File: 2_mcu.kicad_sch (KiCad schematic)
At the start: 24 parts, among them J1 SWD TagConnect

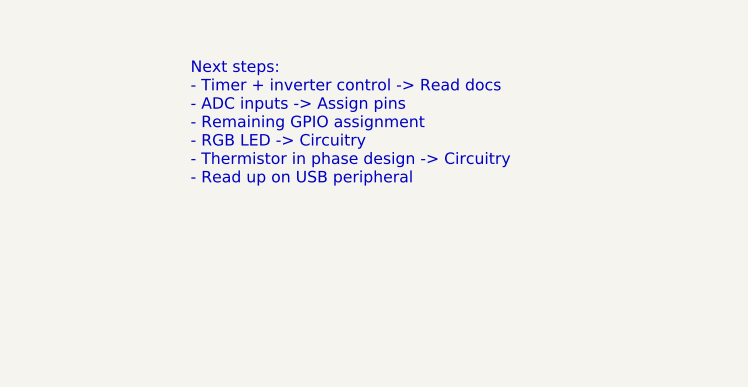
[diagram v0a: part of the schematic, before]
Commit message: verified Timer 1 functionality for motor control
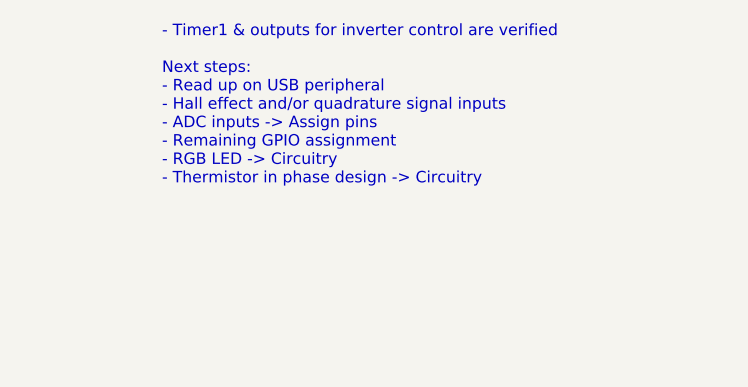
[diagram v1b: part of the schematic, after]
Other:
- note added: "- Timer1 & outputs for inverter control are verified Next steps: - Read up on USB peripheral - Hall effect and/or quadrature signal inputs - ADC inputs -> Assign pins - Remaining GPIO assignment - RGB LED -> Circuitry - Thermistor in phase design -> Circuitry"
- note removed: "Next steps: - Timer + inverter control -> Read docs - ADC inputs -> Assign pins - Remaining GPIO assignment - RGB LED -> Circuitry - Thermistor in phase design -> Circuitry - Read up on USB peripheral"
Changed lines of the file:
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@@
     (effects (font (size 1.6 1.6) italic) (justify left bottom))
   )
-  (text "Next steps:\n- Timer + inverter control -> Read docs\n- ADC inputs -> Assign pins\n- Remaining GPIO assignment\n- RGB LED -> Circuitry\n- Thermistor in phase design -> Circuitry\n- Read up on USB peripheral"
-    (at 234.315 34.925 0)
+  (text "- Timer1 & outputs for inverter control are verified\n\nNext steps:\n- Read up on USB peripheral\n- Hall effect and/or quadrature signal inputs\n- ADC inputs -> Assign pins\n- Remaining GPIO assignment\n- RGB LED -> Circuitry\n- Thermistor in phase design -> Circuitry\n"
+    (at 231.14 34.925 0)
     (effects (font (size 1.27 1.27)) (justify left bottom))
   )

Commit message: feat: USB circuitry
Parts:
- removed D1: ESDALC6V1W5, symbol Power_Protection:ESDALC6V1W5
- added D2: ESDA6V1-5SC6, Package_TO_SOT_SMD:SOT-23-6, symbol Power_Protection:ESDA6V1-5SC6
- added R1: 50R, symbol Device:R_Small
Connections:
- net +3.3V: now also D2.6 (IO5)
- net GND: now also D2.2 (GND); no longer J1.6 (SWO)
- net SYS_SWDIO: now also R1.1
- net at J1.2 (SWDIO), R?.2: now also D2.3 (IO2)
- net at J1.4 (SWCLK), R?.2: now also D2.4 (IO3)
- net at J1.3 (~{RESET}), R?.2: now also D2.5 (IO4)
- new net: D2.1 (IO1), J1.6 (SWO), R1.2
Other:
- note added: "- Timer1 & outputs for inverter control are verified Next steps: - Hall effect and/or quadrature signal inputs - ADC inputs -> Assign pins - Remaining GPIO assignment - RGB LED -> Circuitry - Thermistor in phase design -> Circuitry"
- note removed: "- Timer1 & outputs for inverter control are verified Next steps: - Read up on USB peripheral - Hall effect and/or quadrature signal inputs - ADC inputs -> Assign pins - Remaining GPIO assignment - RGB LED -> Circuitry - Thermistor in phase design -> Circuitry"
- moved on the sheet: C?, L?, R?, SW?, U?, Y?

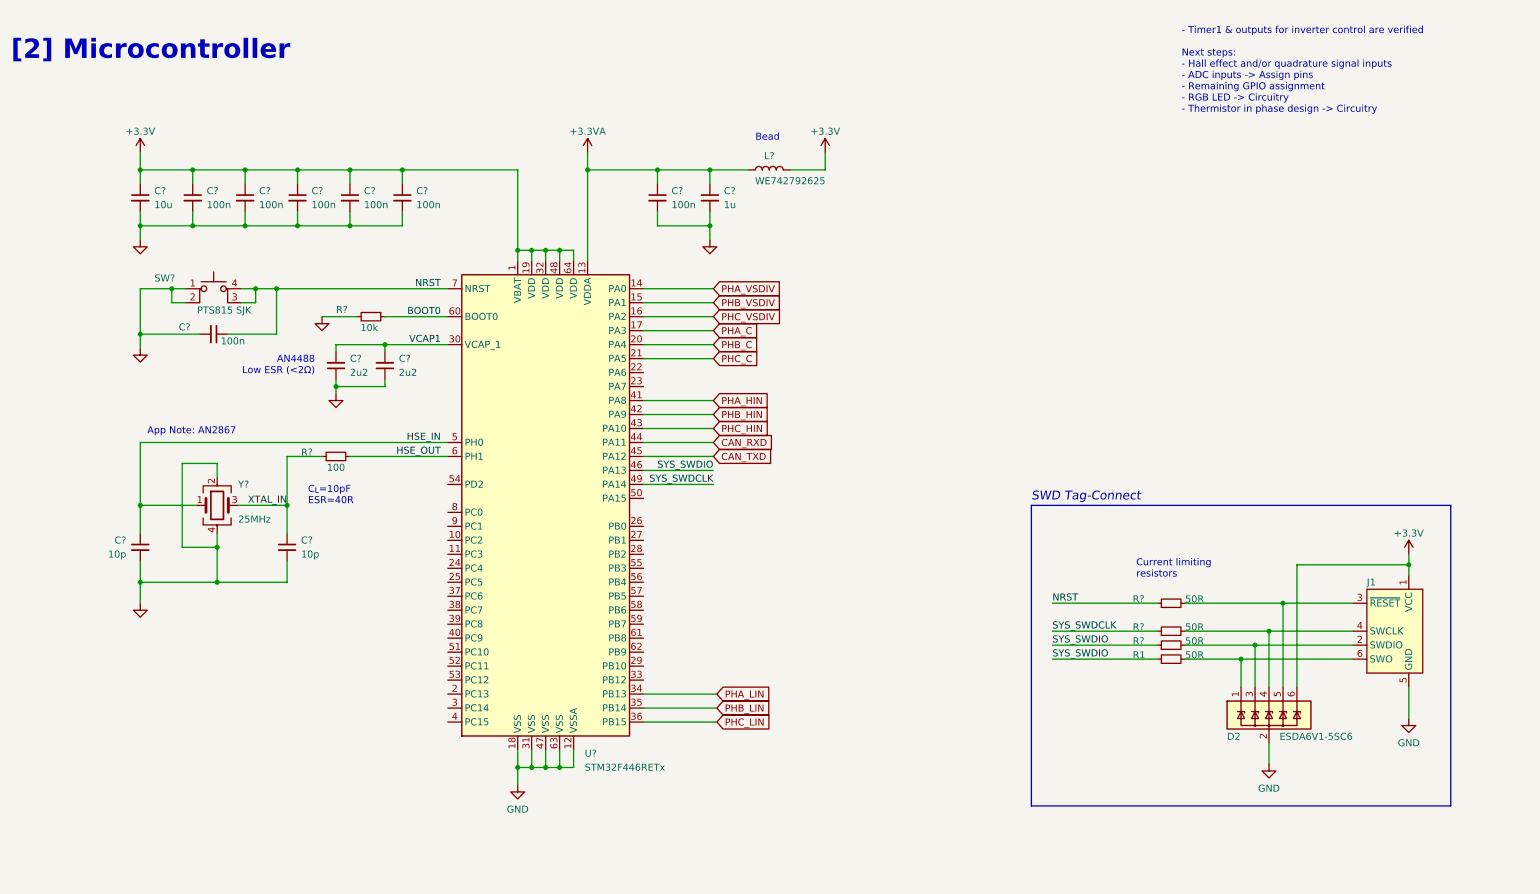
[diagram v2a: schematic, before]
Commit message: chore: updated links and footprints
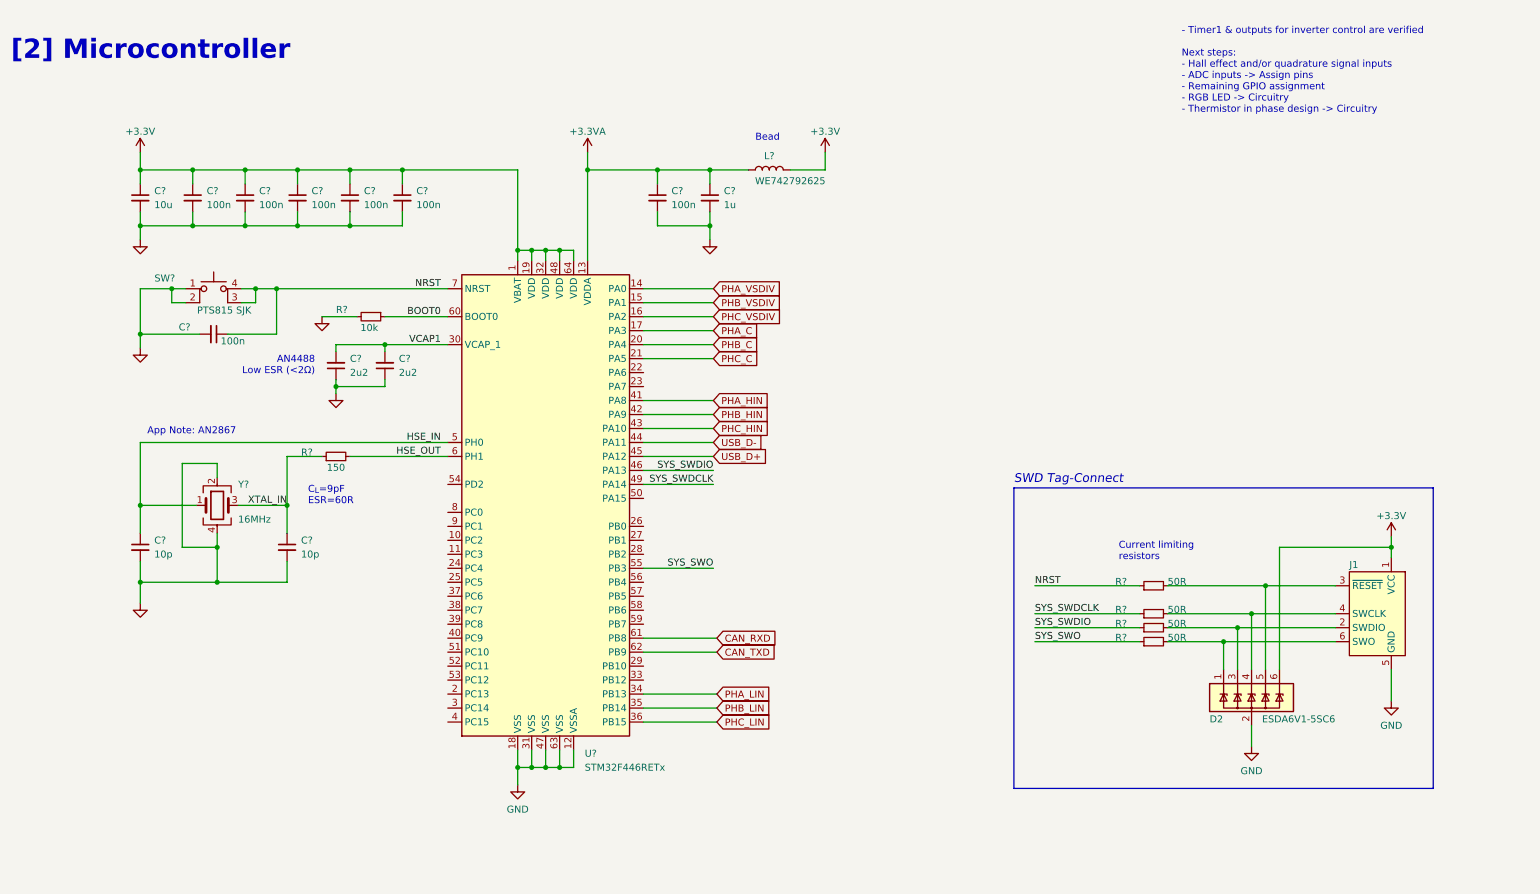
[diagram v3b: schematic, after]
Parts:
- removed C?: 10p, symbol Device:C_Small
- removed R1, R? (x2): 50R, symbol Device:R_Small
- added C?: 10p, Capacitor_SMD:C_0402_1005Metric_Pad0.74x0.62mm_HandSolder, symbol Device:C_Small
- added R? (x3): 50R, Resistor_SMD:R_0402_1005Metric_Pad0.72x0.64mm_HandSolder, symbol Device:R_Small
- C?: footprint (none) -> Capacitor_SMD:C_0402_1005Metric_Pad0.74x0.62mm_HandSolder
- R?: footprint (none) -> Resistor_SMD:R_0402_1005Metric_Pad0.72x0.64mm_HandSolder
- R?: value 100 -> 150; footprint (none) -> Resistor_SMD:R_0402_1005Metric_Pad0.72x0.64mm_HandSolder; Link (none) -> https://www.digikey.de/en/products/detail/yageo/RC0402FR-07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
- U?: Link (none) -> https://www.digikey.com/en/products/detail/stmicroelectroni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
- Y?: value 25MHz -> 16MHz; footprint (none) -> Crystal:Crystal_SMD_SeikoEpson_FA238V-4Pin_3.2x2.5mm; Link (none) -> https://www.digikey.de/en/products/detail/epson/TSX-3225-16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
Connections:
- net CAN_RXD: now also U?.61 (PB8); no longer U?.44 (PA11)
- net CAN_TXD: now also U?.62 (PB9); no longer U?.45 (PA12)
- net GND: now also C?.2
- net HSE_IN: now also C?.1
- net SYS_SWDCLK: now also R?.1
- net SYS_SWDIO: now also R?.1
- net at D2.1 (IO1), J1.6 (SWO): now also R?.2
- net at D2.3 (IO2), J1.2 (SWDIO): now also R?.2
- net at D2.4 (IO3), J1.4 (SWCLK): now also R?.2
- net SYS_SWO: now reaches U?.55 (PB3)
- net SYS_SWO: now also R?.1
- new net USB_D+: U?.45 (PA12)
- new net USB_D-: U?.44 (PA11)
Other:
- note added: "C_{L}=9pF ESR=60R"
- note removed: "C_{L}=10pF ESR=40R"
- moved on the sheet: D2, J1, R?

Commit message: feat: rgb led
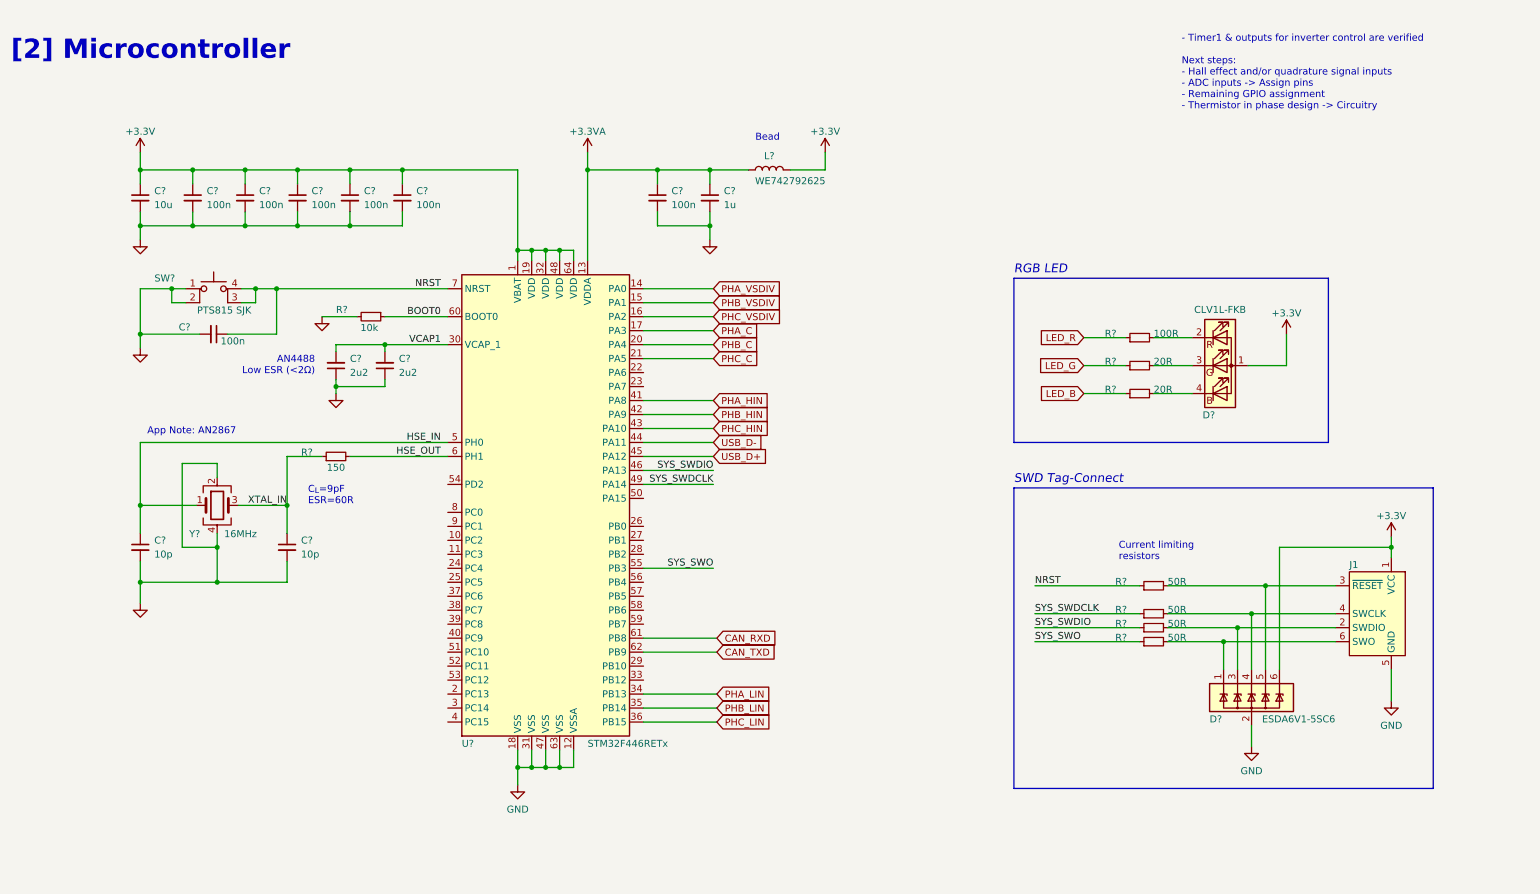
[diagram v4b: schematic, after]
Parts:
- added D?: CLV1L-FKB, LED_SMD:LED_Cree-PLCC4_3.2x2.8mm_CCW, symbol LED:CLV1L-FKB
- added R? (x2): 20R, Resistor_SMD:R_0603_1608Metric_Pad0.98x0.95mm_HandSolder, symbol Device:R_Small
- added R?: 100R, Resistor_SMD:R_0603_1608Metric_Pad0.98x0.95mm_HandSolder, symbol Device:R_Small
- renumbered D2 to D?
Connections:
- net +3.3V: now also D?.1 (A)
- new net: D?.3 (GK), R?.2
- new net: D?.2 (RK), R?.2
- new net: D?.4 (BK), R?.2
- new net LED_B: R?.1
- new net LED_G: R?.1
- new net LED_R: R?.1
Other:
- note added: "- Timer1 & outputs for inverter control are verified Next steps: - Hall effect and/or quadrature signal inputs - ADC inputs -> Assign pins - Remaining GPIO assignment - Thermistor in phase design -> Circuitry"
- note added: "RGB LED"
- note removed: "- Timer1 & outputs for inverter control are verified Next steps: - Hall effect and/or quadrature signal inputs - ADC inputs -> Assign pins - Remaining GPIO assignment - RGB LED -> Circuitry - Thermistor in phase design -> Circuitry"

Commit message: feat: new phases, LED pins
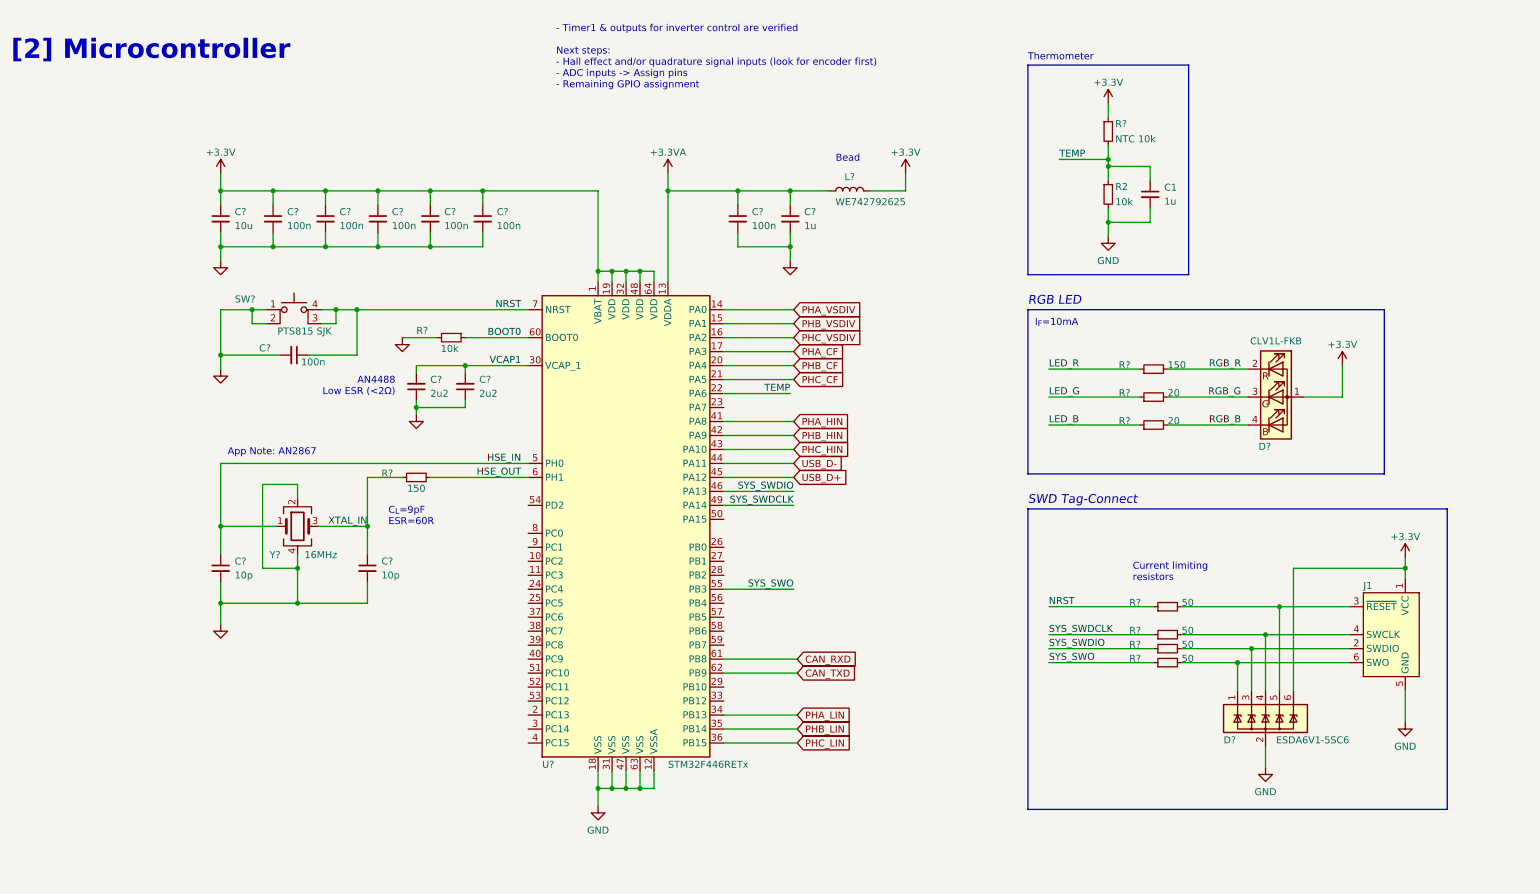
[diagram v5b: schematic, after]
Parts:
- removed R?: 100R, Resistor_SMD:R_0603_1608Metric_Pad0.98x0.95mm_HandSolder, symbol Device:R_Small
- added C1: 1u, Resistor_SMD:R_0603_1608Metric_Pad0.98x0.95mm_HandSolder, symbol Device:C_Small
- added R2: 10k, Resistor_SMD:R_0603_1608Metric_Pad0.98x0.95mm_HandSolder, symbol Device:R_Small
- added R?: NTC 10k, Resistor_SMD:R_0603_1608Metric_Pad0.98x0.95mm_HandSolder, symbol Device:R_Small
- added R?: 150, Resistor_SMD:R_0402_1005Metric_Pad0.72x0.64mm_HandSolder, symbol Device:R_Small
- R? (x2): value 20R -> 20; footprint Resistor_SMD:R_0603_1608Metric_Pad0.98x0.95mm_HandSolder -> Resistor_SMD:R_0402_1005Metric_Pad0.72x0.64mm_HandSolder
- R? (x4): value 50R -> 50
- R?: footprint (none) -> Resistor_SMD:R_0603_1608Metric_Pad0.98x0.95mm_HandSolder
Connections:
- net +3.3V: now also R?.1
- net GND: now also C1.2, R2.2
- net LED_R: now also R?.1
- net RGB_G: now reaches D?.3 (GK), R?.2
- net RGB_R: now reaches D?.2 (RK)
- net RGB_R: now also R?.2
- net RGB_B: now reaches D?.4 (BK), R?.2
- net TEMP: now reaches U?.22 (PA6)
- net TEMP: now also C1.1, R2.1, R?.2
- net PHA_C renamed PHA_CF
- net PHB_C renamed PHB_CF
- net PHC_C renamed PHC_CF
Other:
- note added: "- Timer1 & outputs for inverter control are verified Next steps: - Hall effect and/or quadrature signal inputs (look for encoder first) - ADC inputs -> Assign pins - Remaining GPIO assignment"
- note added: "I_{F}=10mA"
- note added: "Thermometer"
- note removed: "- Timer1 & outputs for inverter control are verified Next steps: - Hall effect and/or quadrature signal inputs - ADC inputs -> Assign pins - Remaining GPIO assignment - Thermistor in phase design -> Circuitry"
- moved on the sheet: C?, D?, J1, L?, R?, SW?, U?, Y?

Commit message: feat: LED routing, encoder interface, footprint updates
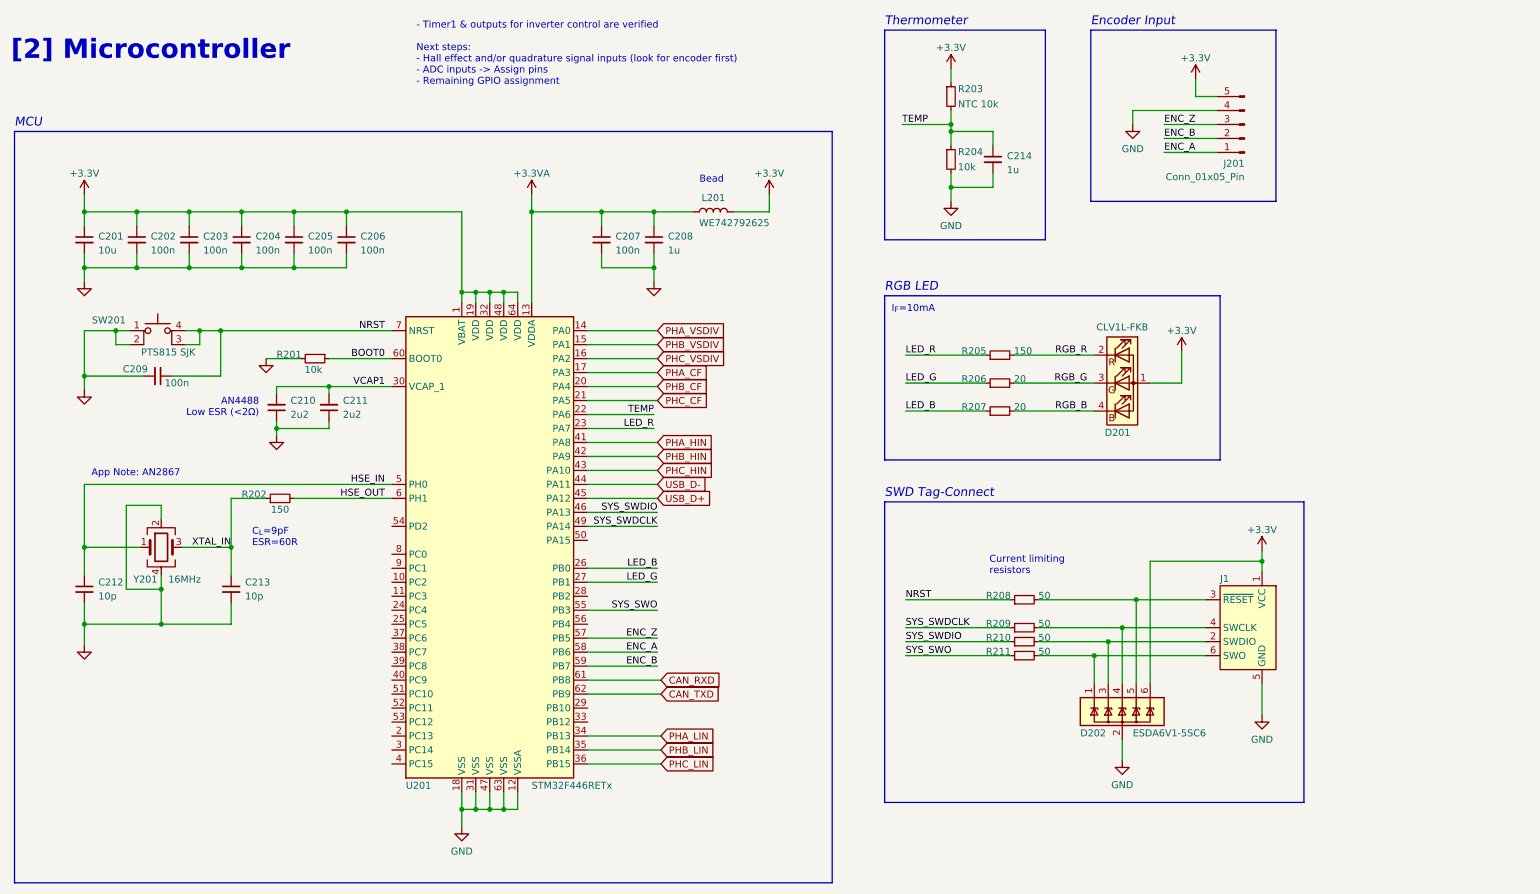
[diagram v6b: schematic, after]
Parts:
- added J201: Conn_01x05_Pin, symbol Connector:Conn_01x05_Pin
- C214: renamed from C1; footprint Resistor_SMD:R_0603_1608Metric_Pad0.98x0.95mm_HandSolder -> (none)
- gave numbers to parts that had none: 29
- renumbered R2 to R204
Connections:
- net +3.3V: now also J201.5 (Pin_5)
- net GND: now also J201.4 (Pin_4)
- net LED_B: now also U201.26 (PB0)
- net LED_G: now also U201.27 (PB1)
- net LED_R: now also U201.23 (PA7)
- net ENC_Z: now reaches U201.57 (PB5)
- net ENC_Z: now also J201.3 (Pin_3)
- net ENC_A: now reaches U201.58 (PB6)
- net ENC_A: now also J201.1 (Pin_1)
- net ENC_B: now reaches U201.59 (PB7)
- net ENC_B: now also J201.2 (Pin_2)
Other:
- note added: "Encoder Input"
- note added: "MCU"
- title: MCU [3] -> MCU
- moved on the sheet: C201, C202, C203, C204, C205, C206, C207, C208, C209, C210, C211, C212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
